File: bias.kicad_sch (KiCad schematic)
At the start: 31 parts, among them Q2001 DPLS350E, Q2002 DNLS350E, Q2003 DPLS350E, Q2004 DPLS350E, Q2005 DNLS350E, Q2006 DNLS350E, Q2007 TIP41C, Q2008 TIP42C

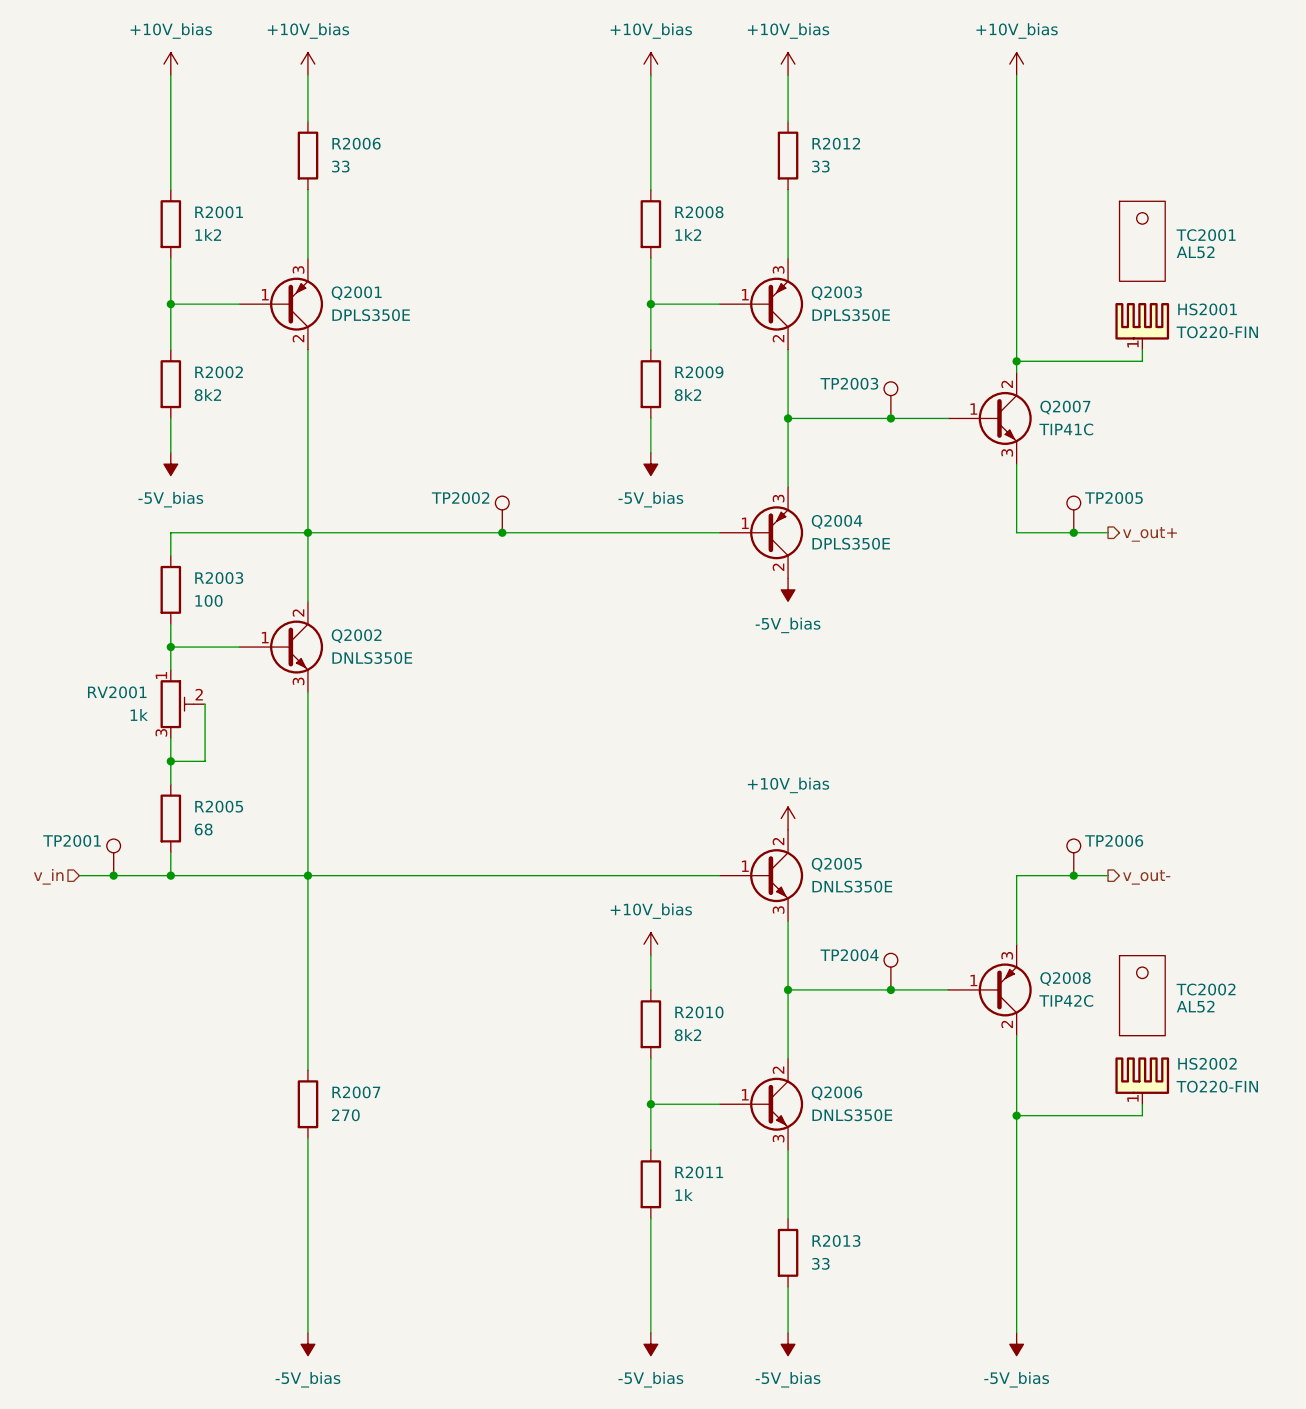
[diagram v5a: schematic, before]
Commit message: edit pss footprint library: export all footprints to library 'pss' and update footprint links
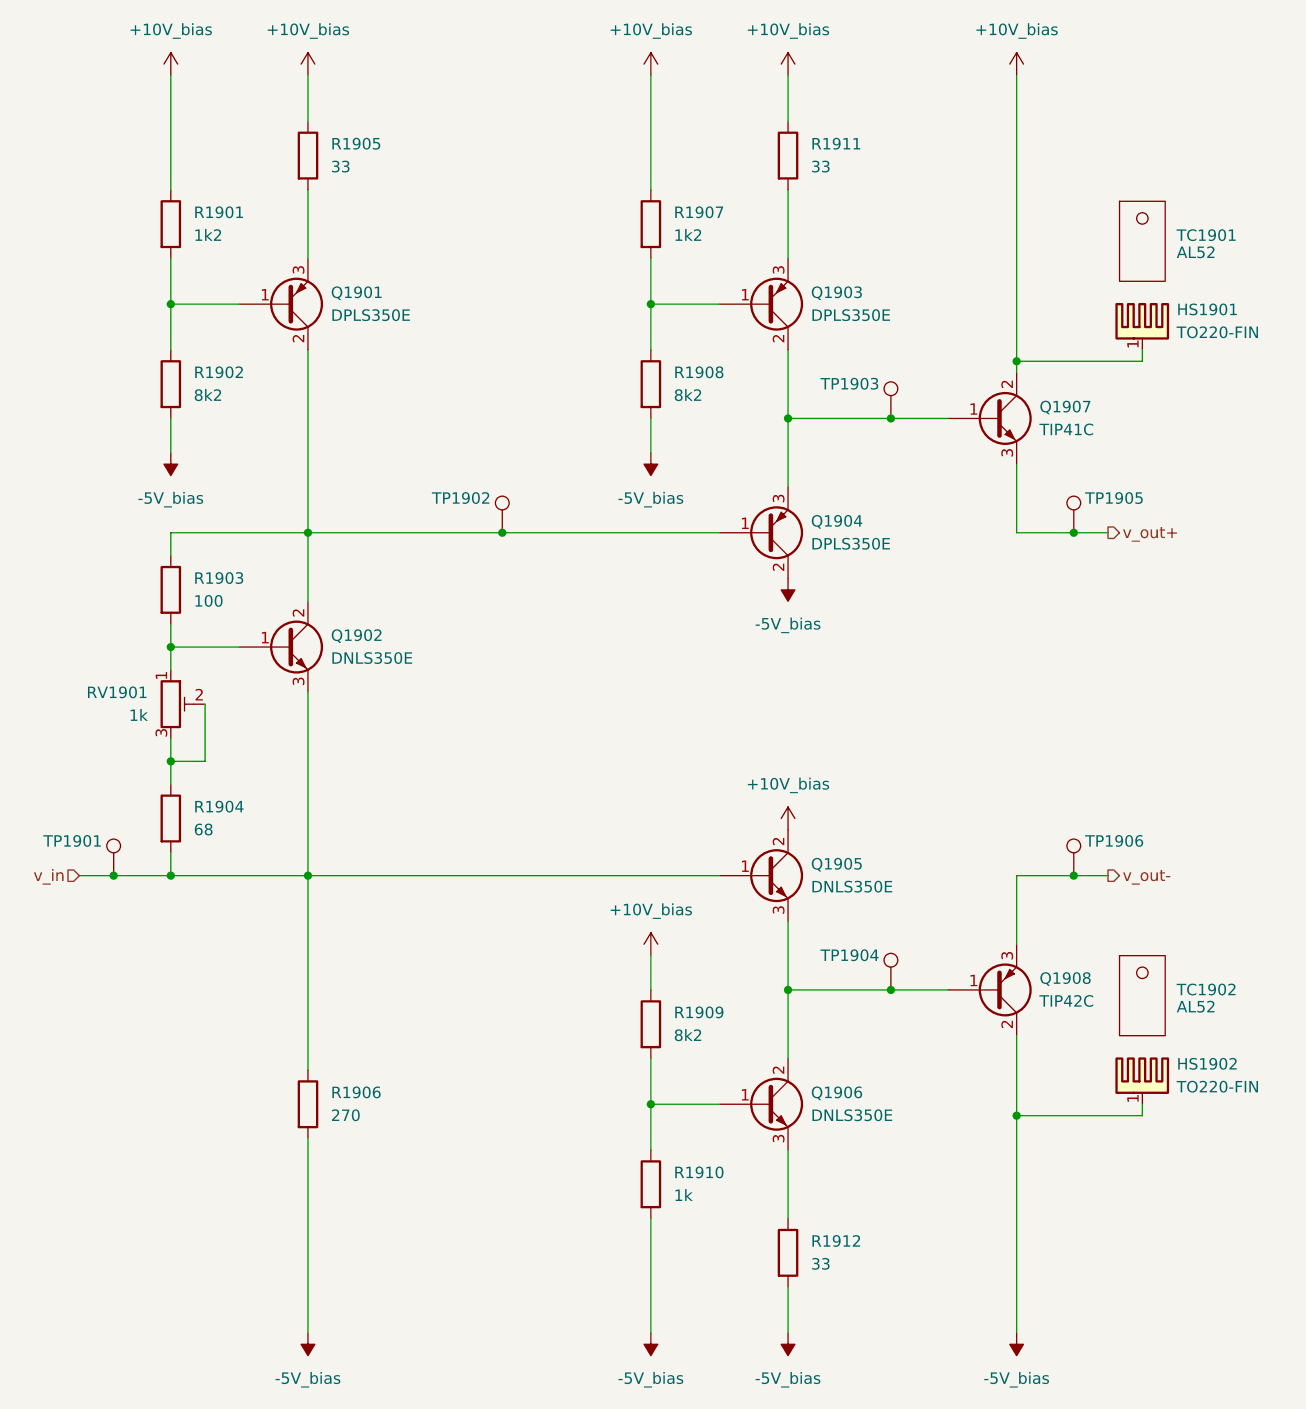
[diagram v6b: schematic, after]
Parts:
- Q1901: renamed from Q2001; footprint Package_TO_SOT_SMD:SOT-223-3_TabPin2 -> pss:SOT-223-3_TabPin2
- Q1902: renamed from Q2002; footprint Package_TO_SOT_SMD:SOT-223-3_TabPin2 -> pss:SOT-223-3_TabPin2
- Q1903: renamed from Q2003; footprint Package_TO_SOT_SMD:SOT-223-3_TabPin2 -> pss:SOT-223-3_TabPin2
- Q1904: renamed from Q2004; footprint Package_TO_SOT_SMD:SOT-223-3_TabPin2 -> pss:SOT-223-3_TabPin2
- Q1905: renamed from Q2005; footprint Package_TO_SOT_SMD:SOT-223-3_TabPin2 -> pss:SOT-223-3_TabPin2
- Q1906: renamed from Q2006; footprint Package_TO_SOT_SMD:SOT-223-3_TabPin2 -> pss:SOT-223-3_TabPin2
- Q1907: renamed from Q2007; footprint Package_TO_SOT_THT:TO-220-3_Vertical -> pss:TO-220-3_Vertical
- Q1908: renamed from Q2008; footprint Package_TO_SOT_THT:TO-220-3_Vertical -> pss:TO-220-3_Vertical
- R1901: renamed from R2001; footprint Resistor_SMD:R_1210_3225Metric_Pad1.30x2.65mm_HandSolder -> pss:R_1210_3225Metric_Pad1.30x2.65mm_HandSolder
- R1902: renamed from R2002; footprint Resistor_SMD:R_1210_3225Metric_Pad1.30x2.65mm_HandSolder -> pss:R_1210_3225Metric_Pad1.30x2.65mm_HandSolder
- R1903: renamed from R2003; footprint Resistor_SMD:R_1210_3225Metric_Pad1.30x2.65mm_HandSolder -> pss:R_1210_3225Metric_Pad1.30x2.65mm_HandSolder
- R1904: renamed from R2005; footprint Resistor_SMD:R_1210_3225Metric_Pad1.30x2.65mm_HandSolder -> pss:R_1210_3225Metric_Pad1.30x2.65mm_HandSolder
- R1905: renamed from R2006; footprint Resistor_SMD:R_1210_3225Metric_Pad1.30x2.65mm_HandSolder -> pss:R_1210_3225Metric_Pad1.30x2.65mm_HandSolder
- R1906: renamed from R2007; footprint Resistor_SMD:R_1210_3225Metric_Pad1.30x2.65mm_HandSolder -> pss:R_1210_3225Metric_Pad1.30x2.65mm_HandSolder
- R1907: renamed from R2008; footprint Resistor_SMD:R_1210_3225Metric_Pad1.30x2.65mm_HandSolder -> pss:R_1210_3225Metric_Pad1.30x2.65mm_HandSolder
- R1908: renamed from R2009; footprint Resistor_SMD:R_1210_3225Metric_Pad1.30x2.65mm_HandSolder -> pss:R_1210_3225Metric_Pad1.30x2.65mm_HandSolder
- R1909: renamed from R2010; footprint Resistor_SMD:R_1210_3225Metric_Pad1.30x2.65mm_HandSolder -> pss:R_1210_3225Metric_Pad1.30x2.65mm_HandSolder
- R1910: renamed from R2011; footprint Resistor_SMD:R_1210_3225Metric_Pad1.30x2.65mm_HandSolder -> pss:R_1210_3225Metric_Pad1.30x2.65mm_HandSolder
- R1911: renamed from R2012; footprint Resistor_SMD:R_1210_3225Metric_Pad1.30x2.65mm_HandSolder -> pss:R_1210_3225Metric_Pad1.30x2.65mm_HandSolder
- R1912: renamed from R2013; footprint Resistor_SMD:R_1210_3225Metric_Pad1.30x2.65mm_HandSolder -> pss:R_1210_3225Metric_Pad1.30x2.65mm_HandSolder
- renumbered HS2001 to HS1901, HS2002 to HS1902, RV2001 to RV1901, TC2001 to TC1901, TC2002 to TC1902, TP2001 to TP1901, TP2002 to TP1902, TP2003 to TP1903, TP2004 to TP1904, TP2005 to TP1905, TP2006 to TP1906
